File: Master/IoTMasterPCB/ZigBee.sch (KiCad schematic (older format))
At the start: 13 parts

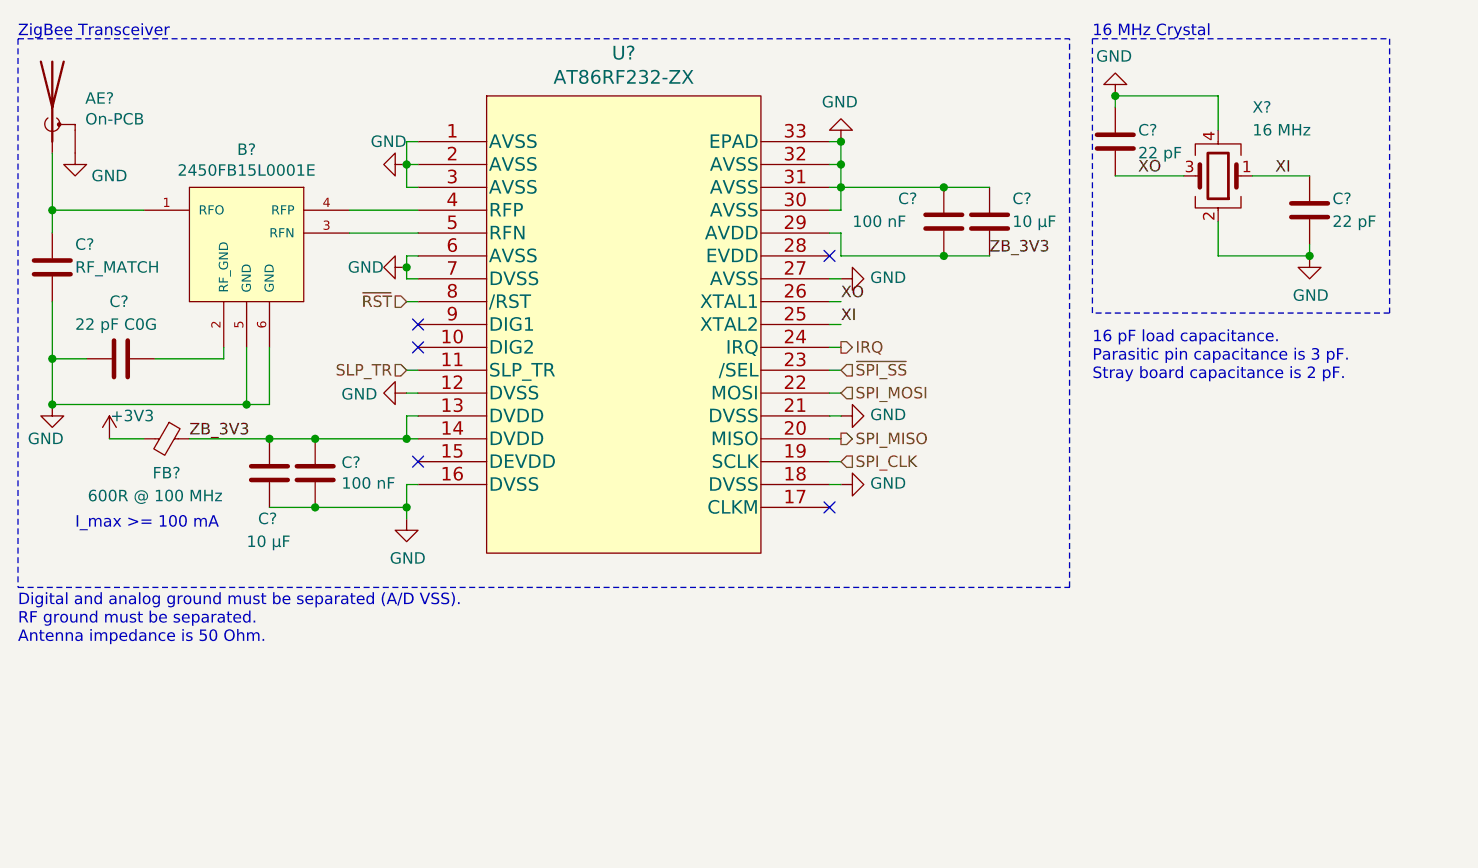
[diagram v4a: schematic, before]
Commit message: Finished RFID and Ethernet circuits.
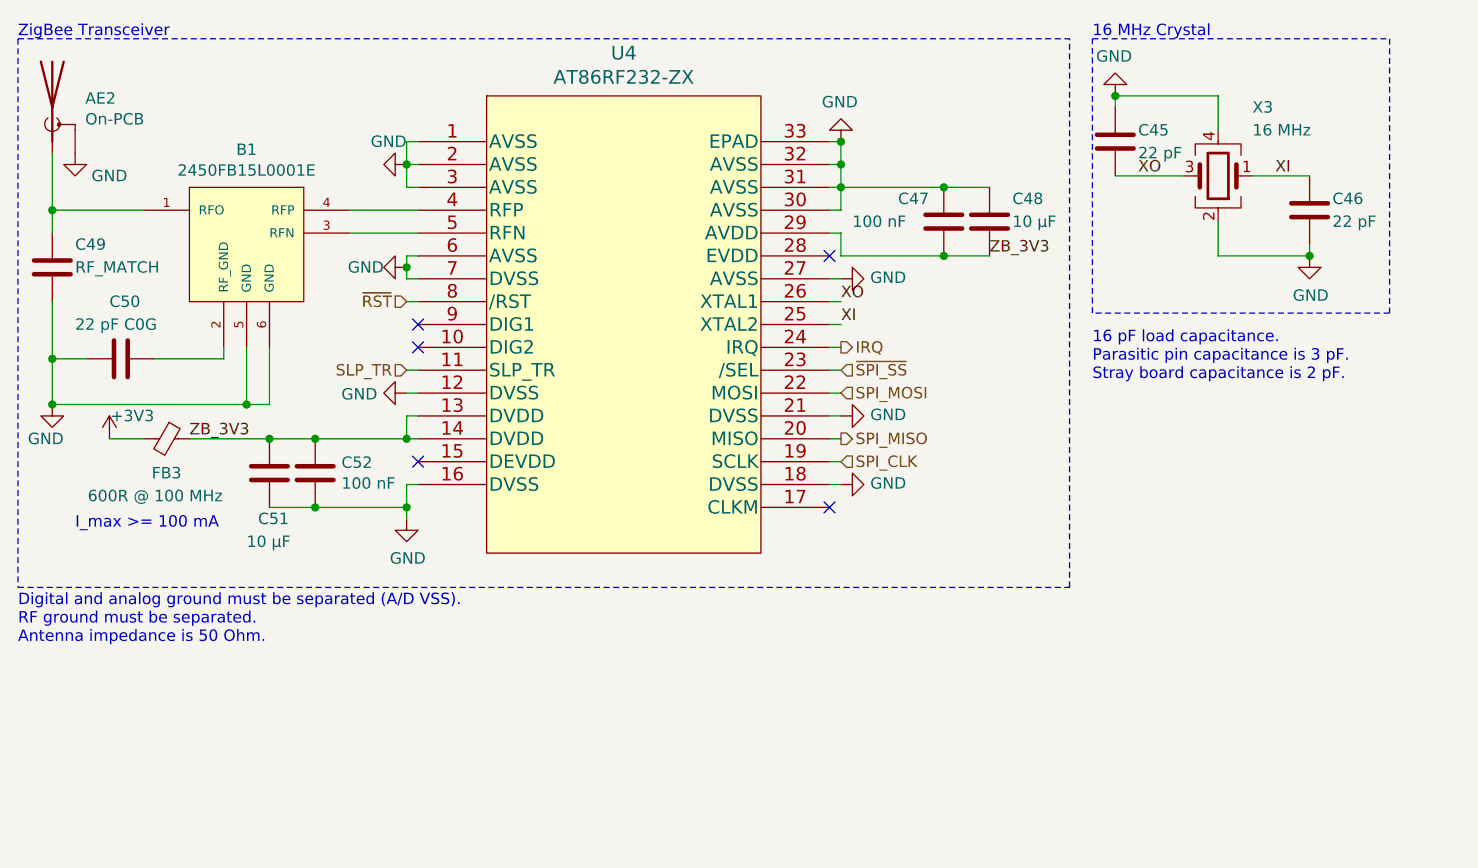
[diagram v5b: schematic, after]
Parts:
- FB3: renamed from FB?; footprint (none) -> Inductor_SMD:L_0603_1608Metric
- gave numbers to parts that had none: 12
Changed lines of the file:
@@
 $EndDescr
 $Comp
-L Personal_ICs:AT86RF232-ZX U?
+L Personal_ICs:AT86RF232-ZX U4
 U 1 1 5FCC5795
 P 2850 1500
-F 0 "U?" H 3750 1887 60  0000 C CNN
+F 0 "U4" H 3750 1887 60  0000 C CNN
 F 1 "AT86RF232-ZX" H 3750 1781 60  0000 C CNN
 F 2 "Personal_ICs:AT86RF232-ZX" H 3750 1740 60  0001 C CNN
@@
 	2800 1500 2850 1500
 $Comp
-L power:GND #PWR?
+L power:GND #PWR0135
 U 1 1 5FCC579C
 P 2800 1600
-F 0 "#PWR?" H 2800 1350 50  0001 C CNN
+F 0 "#PWR0135" H 2800 1350 50  0001 C CNN
 F 1 "GND" V 2700 1600 50  0000 R CNN
 F 2 "" H 2800 1600 50  0001 C CNN
@@
 	2800 1700 2850 1700
 $Comp
-L power:GND #PWR?
+L power:GND #PWR0136
 U 1 1 5FCC57A4
 P 2800 2050
-F 0 "#PWR?" H 2800 1800 50  0001 C CNN
+F 0 "#PWR0136" H 2800 1800 50  0001 C CNN
 F 1 "GND" V 2800 1950 50  0000 R CNN
 F 2 "" H 2800 2050 50  0001 C CNN
@@
 	2800 2050 2800 2100
 $Comp
-L power:GND #PWR?
+L power:GND #PWR0137
 U 1 1 5FCC57B2
 P 2800 2600
-F 0 "#PWR?" H 2800 2350 50  0001 C CNN
+F 0 "#PWR0137" H 2800 2350 50  0001 C CNN
 F 1 "GND" V 2805 2472 50  0000 R CNN
 F 2 "" H 2800 2600 50  0001 C CNN
@@
 	2800 2600 2850 2600
 $Comp
-L power:GND #PWR?
+L power:GND #PWR0138
 U 1 1 5FCC57B9
 P 2800 3150
-F 0 "#PWR?" H 2800 2900 50  0001 C CNN
+F 0 "#PWR0138" H 2800 2900 50  0001 C CNN
 F 1 "GND" H 2805 2977 50  0000 C CNN
 F 2 "" H 2800 3150 50  0001 C CNN
@@
 	2800 3000 2850 3000
 $Comp
-L power:GND #PWR?
+L power:GND #PWR0139
 U 1 1 5FCC57C0
 P 4700 3000
-F 0 "#PWR?" H 4700 2750 50  0001 C CNN
+F 0 "#PWR0139" H 4700 2750 50  0001 C CNN
 F 1 "GND" V 4705 2872 50  0000 R CNN
 F 2 "" H 4700 3000 50  0001 C CNN
@@
 	4700 3000 4650 3000
 $Comp
-L power:GND #PWR?
+L power:GND #PWR0140
 U 1 1 5FCC57C7
 P 4700 2700
-F 0 "#PWR?" H 4700 2450 50  0001 C CNN
+F 0 "#PWR0140" H 4700 2450 50  0001 C CNN
 F 1 "GND" V 4705 2572 50  0000 R CNN
 F 2 "" H 4700 2700 50  0001 C CNN
@@
 	4700 2700 4650 2700
 $Comp
-L power:GND #PWR?
+L power:GND #PWR0141
 U 1 1 5FCC57CE
 P 4700 2100
-F 0 "#PWR?" H 4700 1850 50  0001 C CNN
+F 0 "#PWR0141" H 4700 1850 50  0001 C CNN
 F 1 "GND" V 4705 1972 50  0000 R CNN
 F 2 "" H 4700 2100 50  0001 C CNN
@@
 	4700 1800 4650 1800
 $Comp
-L power:GND #PWR?
+L power:GND #PWR0142
 U 1 1 5FCC57D6
 P 4700 1500
-F 0 "#PWR?" H 4700 1250 50  0001 C CNN
+F 0 "#PWR0142" H 4700 1250 50  0001 C CNN
 F 1 "GND" H 4705 1327 50  0000 C CNN
 F 2 "" H 4700 1500 50  0001 C CNN
@@
 	4700 1600 4700 1700
 $Comp
-L Device:C C?
+L Device:C C47
 U 1 1 5FCC57EF
 P 5150 1850
-F 0 "C?" H 4950 1950 50  0000 L CNN
+F 0 "C47" H 4950 1950 50  0000 L CNN
 F 1 "100 nF" H 4750 1850 50  0000 L CNN
 F 2 "Capacitor_SMD:C_0603_1608Metric" H 5188 1700 50  0001 C CNN
@@
 	2800 2800 2850 2800
 $Comp
-L Device:C C?
+L Device:C C52
 U 1 1 5FCC57FA
 P 2400 2950
-F 0 "C?" H 2515 2996 50  0000 L CNN
+F 0 "C52" H 2515 2996 50  0000 L CNN
 F 1 "100 nF" H 2515 2905 50  0000 L CNN
 F 2 "Capacitor_SMD:C_0603_1608Metric" H 2438 2800 50  0001 C CNN
@@
 	4700 1900 4700 2000
 $Comp
-L Device:Crystal_GND24 X?
+L Device:Crystal_GND24 X3
 U 1 1 5FCC580D
 P 6350 1650
-F 0 "X?" H 6200 1350 50  0000 R CNN
+F 0 "X3" H 6200 1350 50  0000 R CNN
 F 1 "16 MHz" H 6200 1450 50  0000 R CNN
 F 2 "Personal_Actives:ECS1601633BCKMTR" H 6350 1650 50  0001 C CNN
@@
 $EndComp
 $Comp
-L power:GND #PWR?
+L power:GND #PWR0143
 U 1 1 5FCC5813
 P 5900 1300
-F 0 "#PWR?" H 5900 1050 50  0001 C CNN
+F 0 "#PWR0143" H 5900 1050 50  0001 C CNN
 F 1 "GND" H 5905 1127 50  0000 C CNN
 F 2 "" H 5900 1300 50  0001 C CNN
@@
 $EndComp
 $Comp
-L power:GND #PWR?
+L power:GND #PWR0144
 U 1 1 5FCC5819
 P 6750 2000
-F 0 "#PWR?" H 6750 1750 50  0001 C CNN
+F 0 "#PWR0144" H 6750 1750 50  0001 C CNN
 F 1 "GND" H 6755 1827 50  0000 C CNN
 F 2 "" H 6750 2000 50  0001 C CNN
@@
 $EndComp
 $Comp
-L Device:C C?
+L Device:C C46
 U 1 1 5FCC581F
 P 6750 1800
-F 0 "C?" H 6850 1850 50  0000 L CNN
+F 0 "C46" H 6850 1850 50  0000 L CNN
 F 1 "22 pF" H 6850 1750 50  0000 L CNN
 F 2 "Capacitor_SMD:C_0603_1608Metric" H 6788 1650 50  0001 C CNN
@@
 Connection ~ 6750 2000
 $Comp
-L Device:C C?
+L Device:C C45
 U 1 1 5FCC5829
 P 5900 1500
-F 0 "C?" H 6000 1550 50  0000 L CNN
+F 0 "C45" H 6000 1550 50  0000 L CNN
 F 1 "22 pF" H 6000 1450 50  0000 L CNN
 F 2 "Capacitor_SMD:C_0603_1608Metric" H 5938 1350 50  0001 C CNN
@@
 NoConn ~ 2850 2400
 $Comp
-L Device:Antenna_Shield AE?
+L Device:Antenna_Shield AE2
 U 1 1 5FCC5855
 P 1250 1350
-F 0 "AE?" H 1394 1389 50  0000 L CNN
+F 0 "AE2" H 1394 1389 50  0000 L CNN
 F 1 "On-PCB" H 1394 1298 50  0000 L CNN
 F 2 "RF_Antenna:Texas_SWRA117D_2.4GHz_Left" H 1250 1450 50  0001 C CNN
@@
 $EndComp
 $Comp
-L power:GND #PWR?
+L power:GND #PWR0145
 U 1 1 5FCC585B
 P 1350 1550
-F 0 "#PWR?" H 1350 1300 50  0001 C CNN
+F 0 "#PWR0145" H 1350 1300 50  0001 C CNN
 F 1 "GND" H 1500 1450 50  0000 C CNN
 F 2 "" H 1350 1550 50  0001 C CNN
@@
 	2550 1800 2850 1800
 $Comp
-L Personal_Passives:2450FB15L0001E B?
+L Personal_Passives:2450FB15L0001E B1
 U 1 1 5FCC5863
 P 2550 1900
-F 0 "B?" H 3000 1535 50  0000 C CNN
+F 0 "B1" H 3000 1535 50  0000 C CNN
 F 1 "2450FB15L0001E" H 3000 1626 50  0000 C CNN
 F 2 "Personal_Passives:2450FB15L0001E" H 3300 2100 50  0001 L BNN
@@
 $EndComp
 $Comp
-L power:GND #PWR?
+L power:GND #PWR0146
 U 1 1 5FCC5869
 P 1250 2650
-F 0 "#PWR?" H 1250 2400 50  0001 C CNN
+F 0 "#PWR0146" H 1250 2400 50  0001 C CNN
 F 1 "GND" H 1300 2500 50  0000 R CNN
 F 2 "" H 1250 2650 50  0001 C CNN
@@
 	1250 1800 1250 1550
 $Comp
-L Device:C C?
+L Device:C C50
 U 1 1 5FCC5872
 P 1550 2450
-F 0 "C?" V 1300 2400 50  0000 L CNN
+F 0 "C50" V 1300 2400 50  0000 L CNN
 F 1 "22 pF C0G" V 1400 2250 50  0000 L CNN
 F 2 "Capacitor_SMD:C_0402_1005Metric" H 1588 2300 50  0001 C CNN
@@
 Connection ~ 2100 2650
 $Comp
-L Device:C C?
+L Device:C C49
 U 1 1 5FCC5883
 P 1250 2050
-F 0 "C?" H 1350 2150 50  0000 L CNN
+F 0 "C49" H 1350 2150 50  0000 L CNN
 F 1 "RF_MATCH" H 1350 2050 50  0000 L CNN
 F 2 "Capacitor_SMD:C_0805_2012Metric" H 1288 1900 50  0001 C CNN
@@
 Connection ~ 1250 2450
 $Comp
-L Device:C C?
+L Device:C C48
 U 1 1 5FCC588D
 P 5350 1850
-F 0 "C?" H 5450 1950 50  0000 L CNN
+F 0 "C48" H 5450 1950 50  0000 L CNN
 F 1 "10 µF" H 5450 1850 50  0000 L CNN
 F 2 "Capacitor_SMD:C_0805_2012Metric" H 5388 1700 50  0001 C CNN
@@
 Connection ~ 5150 1700
 $Comp
-L Device:C C?
+L Device:C C51
 U 1 1 5FCC5899
 P 2200 2950
-F 0 "C?" H 2150 2750 50  0000 L CNN
+F 0 "C51" H 2150 2750 50  0000 L CNN
 F 1 "10 µF" H 2100 2650 50  0000 L CNN
 F 2 "Capacitor_SMD:C_0805_2012Metric" H 2238 2800 50  0001 C CNN
@@
 	1850 2800 2200 2800
 $Comp
-L power:+3V3 #PWR?
+L power:+3V3 #PWR0147
 U 1 1 5FCC9953
 P 1500 2800
-F 0 "#PWR?" H 1500 2650 50  0001 C CNN
+F 0 "#PWR0147" H 1500 2650 50  0001 C CNN
 F 1 "+3V3" H 1600 2900 50  0000 C CNN
 F 2 "" H 1500 2800 50  0001 C CNN
@@
 $EndComp
 $Comp
-L Device:Ferrite_Bead_Small FB?
+L Device:Ferrite_Bead_Small FB3
 U 1 1 5FE2F067
 P 1750 2800
-F 0 "FB?" V 1900 2800 50  0000 C CNN
+F 0 "FB3" V 1900 2800 50  0000 C CNN
 F 1 "600R @ 100 MHz" V 2000 2750 50  0000 C CNN
-F 2 "" V 1680 2800 50  0001 C CNN
-F 3 "~" H 1750 2800 50  0001 C CNN
+F 2 "Inductor_SMD:L_0603_1608Metric" V 1680 2800 50  0001 C CNN
+F 3 "https://www.mouser.dk/ProductDetail/Murata-Electronics/BLM18KG102SN1D?qs=sGAEpiMZZMt1hubY80%2Fs8DE23zOR%2FvJ9bRjl4ASn6yNa9y2qgnK%2Fqg%3D%3D" H 1750 2800 50  0001 C CNN
 	1    1750 2800
 	0    1    1    0
